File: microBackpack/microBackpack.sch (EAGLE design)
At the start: 88 parts, among them IC1 LM324D, IC2 LM324D, J2 USB_B_PTH, J4 2X6 FEMALE, U1 ATMEGA328P_TQFP, U10 TLP185, U11 TLP185, U2 5VREG-HS, U3 CP2102N-QFN24, U4 TVS_DIODE_4PK, U5 MCP4728, U6 78L09F, U7 TVS_DIODE_4PK, U8 TVS_DIODE_4PK, U9 TVS_DIODE_4PK

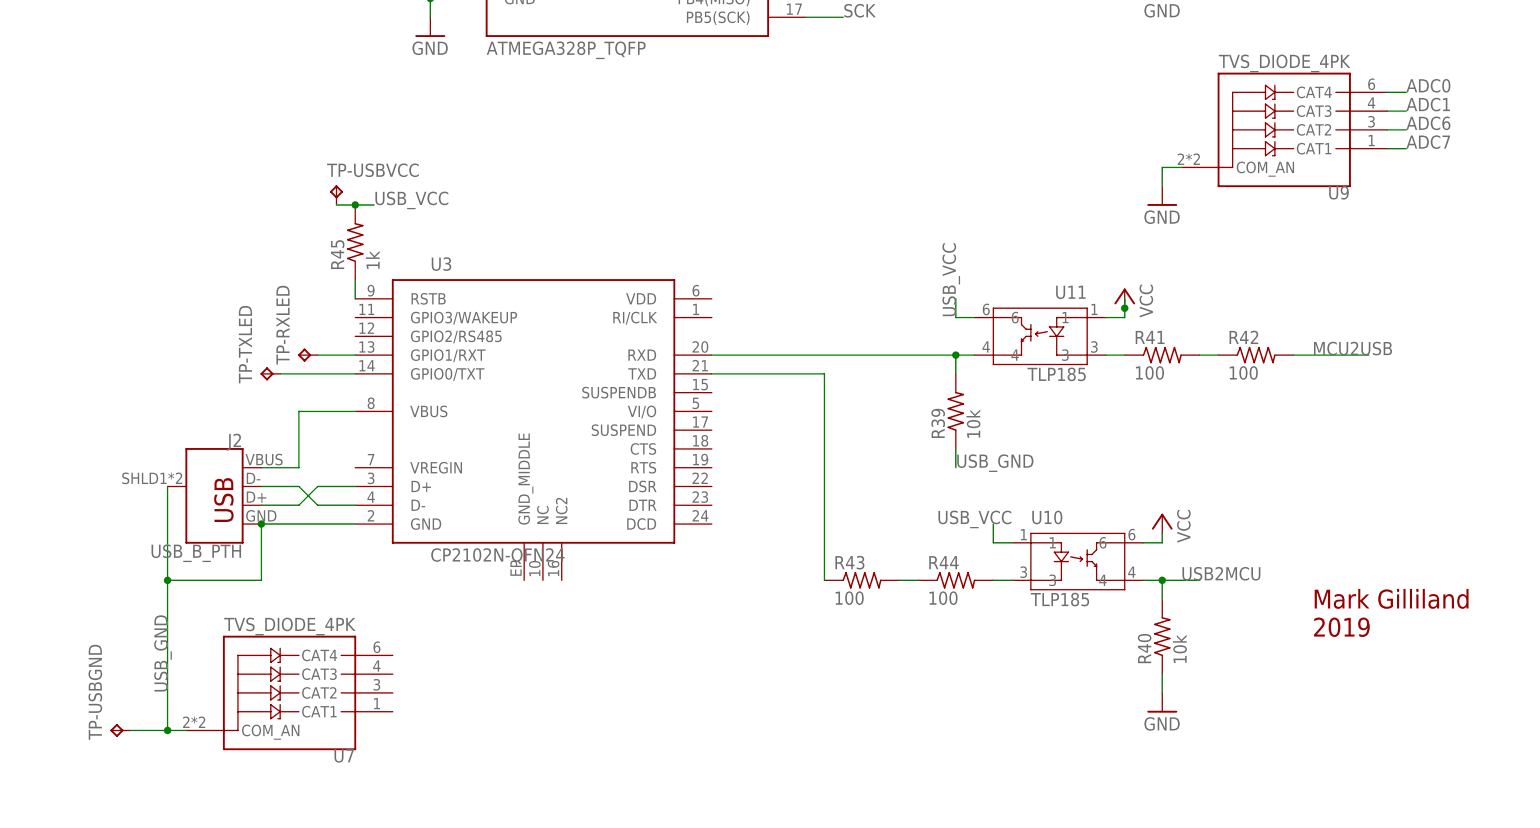
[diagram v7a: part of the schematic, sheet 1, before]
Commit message: Added usb power. Switched optocouplers to active-high
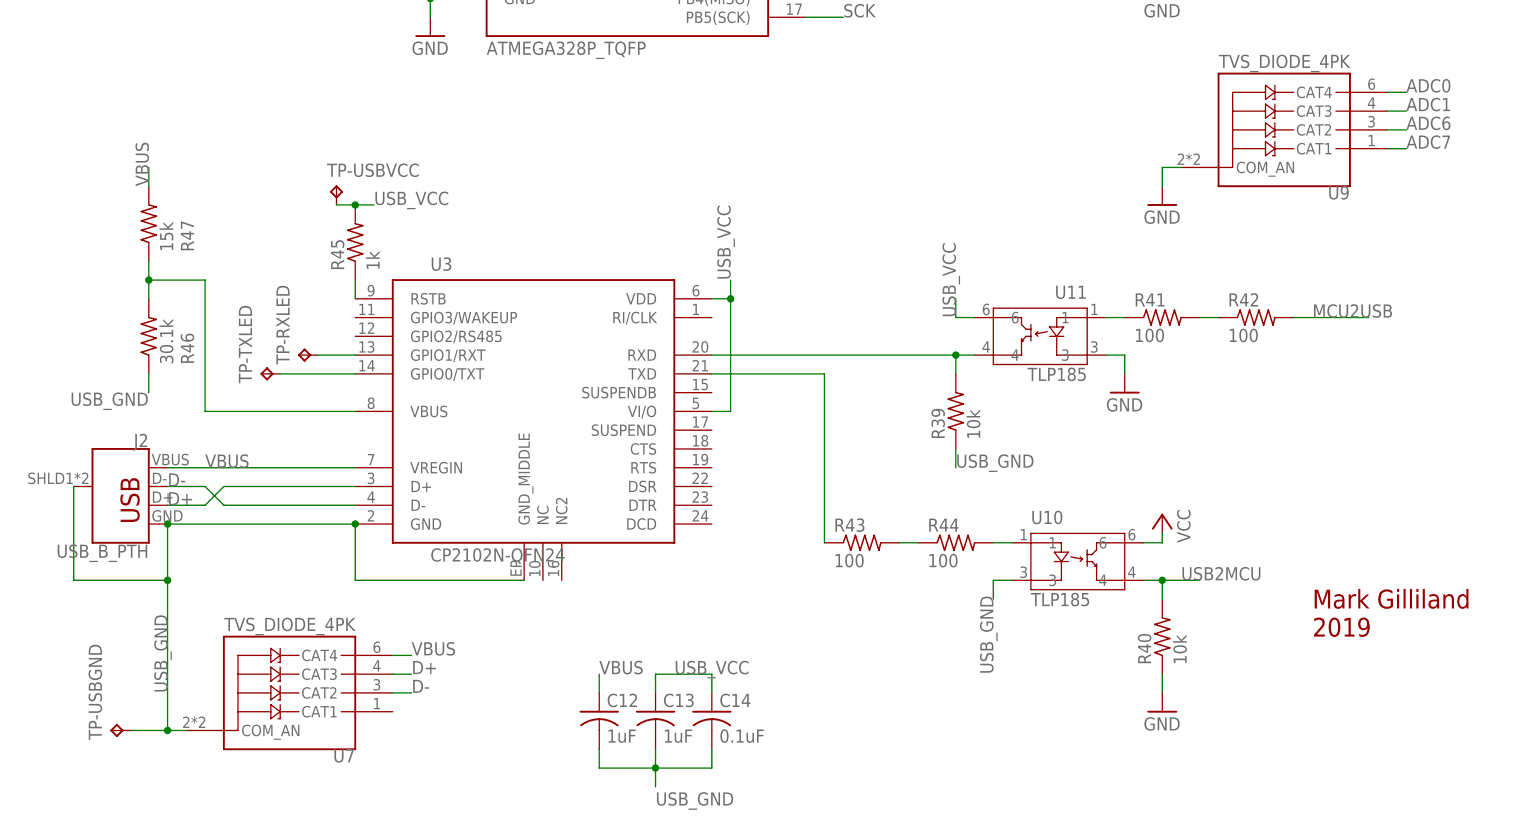
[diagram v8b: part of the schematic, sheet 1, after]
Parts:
- added C12, C13: 1uF, rcl:C-USC0805
- added C14: 0.1uF, rcl:C-USC0805
- added R46: 30.1k, rcl:R-US_R0805
- added R47: 15k, rcl:R-US_R0805
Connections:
- removed net N$18: R44.2, U10.3
- removed net N$19: R41.1, U11.3
- new net D+: J2.D+, U3.D+, U7.CAT3
- new net D-: J2.D-, U3.D-, U7.CAT2
- new net VBUS: C12.1, J2.VBUS, R47.2, U3.VREGIN, U7.CAT4
- net GND: now also U11.3
- net N$5: now also R41.1, U11.1; no longer J2.VBUS, U3.VBUS
- net N$7: now also R46.2, R47.1, U3.VBUS; no longer J2.D-, U3.D-
- net N$8: now also R44.2, U10.1; no longer J2.D+, U3.D+
- net USB_GND: now also C12.2, C13.2, C14.2, R46.1, U10.3, U3.GND_MIDDLE
- net USB_VCC: now also C13.1, C14.1, U3.VDD, U3.VI/O; no longer U10.1
- net VCC: no longer U11.1
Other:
- moved on the sheet: J2, R41, R42, R43, R44
